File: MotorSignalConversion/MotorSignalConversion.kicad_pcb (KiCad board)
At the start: 2 copper layers, 100 x 84.7 mm, 30 parts, among them J1 Conn_01x06_MountingPin, J2 Conn_01x02, J3 Conn_01x06_MountingPin, J5 Conn_01x02, U1 SC0915, U2 MCP4725xxx-xCH, U3 MCP4725xxx-xCH, U4 LM324, U5 LSF0102DCUR

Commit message: added vials to fix ground
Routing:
- net unconnected-(J3-MountPin-PadMP): track 0.00 -> 14.7 mm
- net unconnected-(J1-MountPin-PadMP): track 0.00 -> 14.7 mm
- net /Enable: track 117.6 -> 116.3 mm
- net /GND: vias 3 -> 8
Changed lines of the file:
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@@
+	)
+	(via
+		(at 200.5 110.5)
+		(size 0.6)
+		(drill 0.3)
+		(layers "F.Cu" "B.Cu")
+		(free yes)
+		(net 2)
+	)
+	(via
+		(at 188 100.5)
+		(size 0.6)
+		(drill 0.3)
+		(layers "F.Cu" "B.Cu")
+		(free yes)
+		(net 2)
 	)
 	(via
@@
 	)
 	(via
+		(at 199 109)
+		(size 0.6)
+		(drill 0.3)
+		(layers "F.Cu" "B.Cu")
+		(free yes)
+		(net 2)
+	)
+	(via
+		(at 210 108.5)
+		(size 0.6)
+		(drill 0.3)
+		(layers "F.Cu" "B.Cu")
+		(free yes)
+		(net 2)
+	)
+	(via
+		(at 208 109.5)
+		(size 0.6)
+		(drill 0.3)
+		(layers "F.Cu" "B.Cu")
+		(free yes)
+		(net 2)
+	)
+	(via
 		(at 192 110)
 		(size 0.6)
@@
 		(layers "F.Cu" "B.Cu")
 		(net 2)
+	)
+	(segment
+		(start 157.65 130.4)
+		(end 172.35 130.4)
+		(width 0.2)
+		(layer "F.Cu")
+		(net 3)
 	)
 	(segment
@@
 	)
 	(segment
-		(start 165 130)
-		(end 163.6 130)
-		(width 0.2)
-		(layer "F.Cu")
-		(net 7)
-	)
-	(segment
 		(start 181.43 88.93)
 		(end 185.31 88.93)
@@
 	)
 	(segment
+		(start 160 124.65)
+		(end 160 122.9)
+		(width 0.2)
+		(layer "F.Cu")
+		(net 7)
+	)
+	(segment
 		(start 177.5 125)
 		(end 175 127.5)
@@
 	)
 	(segment
-		(start 160 124.65)
-		(end 160 122.9)
+		(start 167.5 127.5)
+		(end 166.5 128.5)
+		(width 0.2)
+		(layer "F.Cu")
+		(net 7)
+	)
+	(segment
+		(start 175 127.5)
+		(end 167.5 127.5)
+		(width 0.2)
+		(layer "F.Cu")
+		(net 7)
+	)
+	(segment
+		(start 160 122.9)
+		(end 157.1 120)
+		(width 0.2)
+		(layer "F.Cu")
+		(net 7)
+	)
+	(segment
+		(start 157.1 120)
+		(end 150 120)
+		(width 0.2)
+		(layer "F.Cu")
+		(net 7)
+	)
+	(segment
+		(start 166.5 128.5)
+		(end 162.1 128.5)
+		(width 0.2)
+		(layer "F.Cu")
+		(net 7)
+	)
+	(segment
+		(start 184.3 125)
+		(end 177.5 125)
+		(width 0.2)
+		(layer "F.Cu")
+		(net 7)
+	)
+	(segment
+		(start 185 124.3)
+		(end 184.3 125)
 		(width 0.2)
 		(layer "F.Cu")
@@
 	)
 	(segment
-		(start 160 122.9)
-		(end 157.1 120)
-		(width 0.2)
-		(layer "F.Cu")
-		(net 7)
-	)
-	(segment
-		(start 175 127.5)
-		(end 167.5 127.5)
-		(width 0.2)
-		(layer "F.Cu")
-		(net 7)
-	)
-	(segment
-		(start 157.1 120)
-		(end 150 120)
-		(width 0.2)
-		(layer "F.Cu")
-		(net 7)
-	)
-	(segment
-		(start 167.5 127.5)
-		(end 165 130)
-		(width 0.2)
-		(layer "F.Cu")
-		(net 7)
-	)
-	(segment
-		(start 163.6 130)
+		(start 162.1 128.5)
 		(end 160 126.4)
-		(width 0.2)
-		(layer "F.Cu")
-		(net 7)
-	)
-	(segment
-		(start 185 124.3)
-		(end 184.3 125)
-		(width 0.2)
-		(layer "F.Cu")
-		(net 7)
-	)
-	(segment
-		(start 184.3 125)
-		(end 177.5 125)
 		(width 0.2)
 		(layer "F.Cu")
@@
 	)
 	(segment
+		(start 182.65 130.05)
+		(end 197.35 130.05)
+		(width 0.2)
+		(layer "F.Cu")
+		(net 10)
+	)
+	(segment

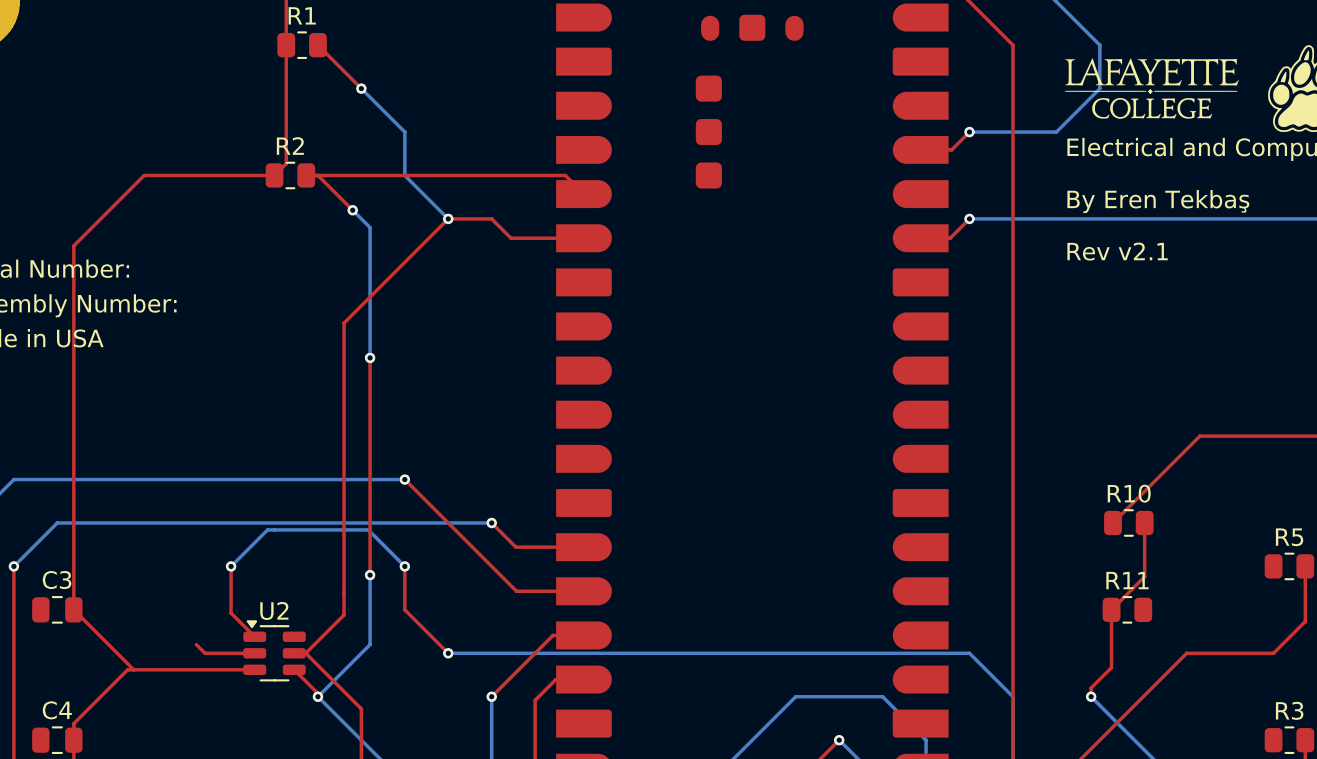
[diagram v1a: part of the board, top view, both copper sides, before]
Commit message: Fixed unconnected ground
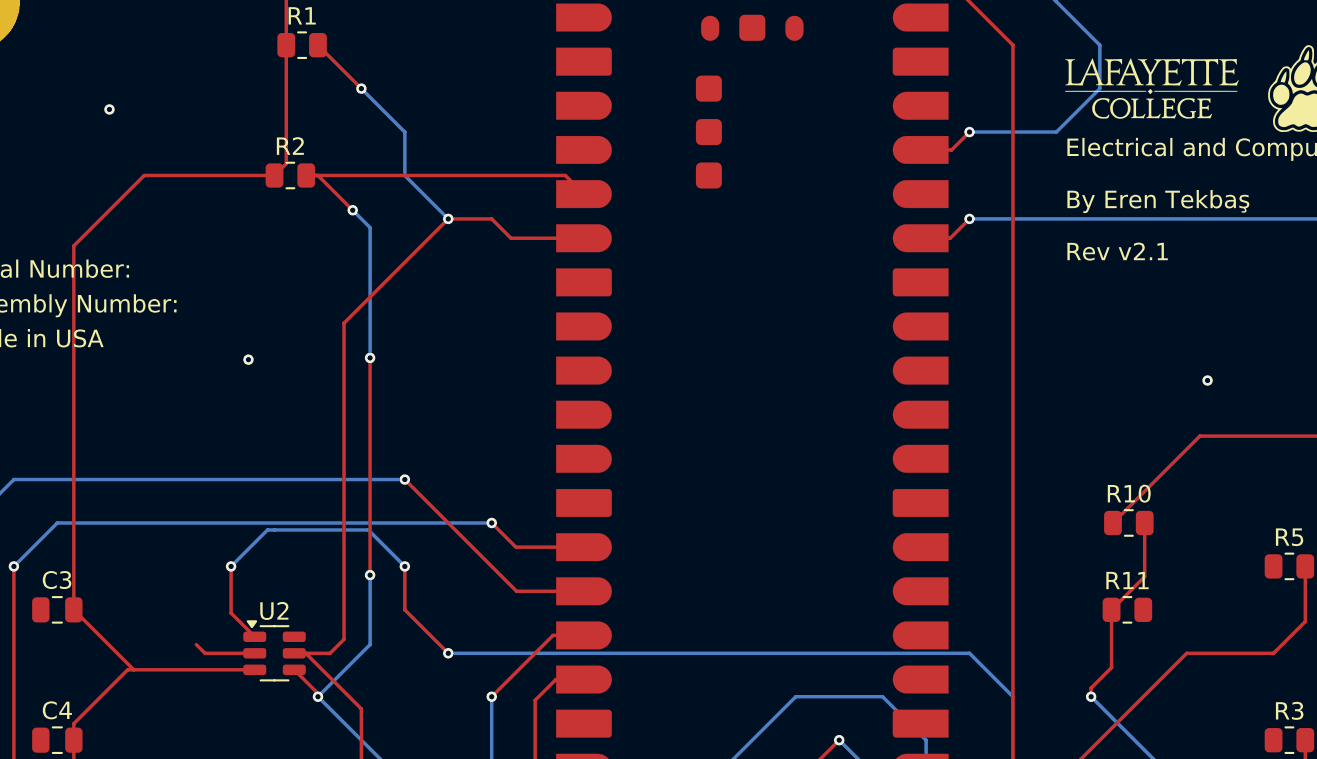
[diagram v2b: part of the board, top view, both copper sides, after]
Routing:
- net /I2C SCL: track 68.7 -> 69.6 mm
- net /GND: vias 8 -> 11
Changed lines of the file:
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@@
 			(size 5.7 5.7)
 			(drill 3.2)
-			(layers "*.Cu" "*.Mask")
+			(layers "*.Cu" "*.Mask" "In1.Cu" "In2.Cu" "In3.Cu" "In4.Cu" "In5.Cu" "In6.Cu"
+				"In7.Cu" "In8.Cu" "In9.Cu" "In10.Cu" "In11.Cu" "In12.Cu" "In13.Cu" "In14.Cu"
+				"In15.Cu" "In16.Cu" "In17.Cu" "In18.Cu" "In19.Cu" "In20.Cu" "In21.Cu"
+				"In22.Cu" "In23.Cu" "In24.Cu" "In25.Cu" "In26.Cu" "In27.Cu" "In28.Cu"
+				"In29.Cu" "In30.Cu"
+			)
 			(remove_unused_layers no)
 		)
@@
 			(size 5.7 5.7)
 			(drill 3.2)
-			(layers "*.Cu" "*.Mask")
+			(layers "*.Cu" "*.Mask" "In1.Cu" "In2.Cu" "In3.Cu" "In4.Cu" "In5.Cu" "In6.Cu"
+				"In7.Cu" "In8.Cu" "In9.Cu" "In10.Cu" "In11.Cu" "In12.Cu" "In13.Cu" "In14.Cu"
+				"In15.Cu" "In16.Cu" "In17.Cu" "In18.Cu" "In19.Cu" "In20.Cu" "In21.Cu"
+				"In22.Cu" "In23.Cu" "In24.Cu" "In25.Cu" "In26.Cu" "In27.Cu" "In28.Cu"
+				"In29.Cu" "In30.Cu"
+			)
 			(remove_unused_layers no)
 		)
@@
 		(tags "connector JST PH vertical")
 		(property "Reference" "J5"
-			(at -6.6 0.5 360)
+			(at -6.6 0.5 0)
 			(layer "F.SilkS")
 			(effects
@@
 		)
 		(property "Value" "Conn_01x02"
-			(at 0 4.45 360)
+			(at 0 4.45 0)
 			(layer "F.Fab")
 			(effects
@@
 		)
 		(fp_text user "${REFERENCE}"
-			(at 0 -1 360)
+			(at 0 -1 0)
 			(layer "F.Fab")
 			(effects
@@
 			(size 5.7 5.7)
 			(drill 3.2)
-			(layers "*.Cu" "*.Mask")
+			(layers "*.Cu" "*.Mask" "In1.Cu" "In2.Cu" "In3.Cu" "In4.Cu" "In5.Cu" "In6.Cu"
+				"In7.Cu" "In8.Cu" "In9.Cu" "In10.Cu" "In11.Cu" "In12.Cu" "In13.Cu" "In14.Cu"
+				"In15.Cu" "In16.Cu" "In17.Cu" "In18.Cu" "In19.Cu" "In20.Cu" "In21.Cu"
+				"In22.Cu" "In23.Cu" "In24.Cu" "In25.Cu" "In26.Cu" "In27.Cu" "In28.Cu"
+				"In29.Cu" "In30.Cu"
+			)
 			(remove_unused_layers no)
 		)
@@
 			(size 5.7 5.7)
 			(drill 3.2)
-			(layers "*.Cu" "*.Mask")
+			(layers "*.Cu" "*.Mask" "In1.Cu" "In2.Cu" "In3.Cu" "In4.Cu" "In5.Cu" "In6.Cu"
+				"In7.Cu" "In8.Cu" "In9.Cu" "In10.Cu" "In11.Cu" "In12.Cu" "In13.Cu" "In14.Cu"
+				"In15.Cu" "In16.Cu" "In17.Cu" "In18.Cu" "In19.Cu" "In20.Cu" "In21.Cu"
+				"In22.Cu" "In23.Cu" "In24.Cu" "In25.Cu" "In26.Cu" "In27.Cu" "In28.Cu"
+				"In29.Cu" "In30.Cu"
+			)
 			(remove_unused_layers no)
 		)
@@
 	)
 	(via
+		(at 158 61.2)
+		(size 0.6)
+		(drill 0.3)
+		(layers "F.Cu" "B.Cu")
+		(free yes)
+		(net 2)
+	)
+	(via
+		(at 221.2 76.8)
+		(size 0.6)
+		(drill 0.3)
+		(layers "F.Cu" "B.Cu")
+		(free yes)
+		(net 2)
+	)
+	(via
+		(at 166 75.6)
+		(size 0.6)
+		(drill 0.3)
+		(layers "F.Cu" "B.Cu")
+		(free yes)
+		(net 2)
+	)
+	(via
 		(at 164 107.5)
 		(size 0.6)
@@
 	)
 	(segment
-		(start 171.5 73.5)
-		(end 171.5 89)
-		(width 0.2)
-		(layer "F.Cu")
-		(net 12)
-	)
-	(segment
 		(start 172.5 95.700001)
 		(end 169.299999 92.5)
@@
 	)
 	(segment
-		(start 171.5 90.299999)
-		(end 169.299999 92.5)
+		(start 171.5 91.7)
+		(end 170.7 92.5)
 		(width 0.2)
 		(layer "F.Cu")
@@
 	)
 	(segment
-		(start 171.5 89)
-		(end 171.5 90.299999)
+		(start 169.299999 107.5)
+		(end 172.5 104.299999)
 		(width 0.2)
 		(layer "F.Cu")
@@
 	)
 	(segment
-		(start 169.299999 107.5)
-		(end 172.5 104.299999)
+		(start 181.11 68.61)
+		(end 185.31 68.61)
 		(width 0.2)
 		(layer "F.Cu")
@@
 	)
 	(segment
-		(start 181.11 68.61)
-		(end 185.31 68.61)
+		(start 170.7 92.5)
+		(end 169.299999 92.5)
 		(width 0.2)
 		(layer "F.Cu")
@@
 	)
 	(segment
+		(start 171.5 73.5)
+		(end 171.5 91.7)
+		(width 0.2)
+		(layer "F.Cu")
+		(net 12)
+	)
+	(segment
 		(start 168.6375 107.5)
 		(end 169.299999 107.5)
@@
 		(net 2)
 		(net_name "/GND")
-		(layers "F&B.Cu")
+		(layers "F.Cu" "B.Cu")
 		(hatch edge 0.5)
 		(connect_pads
